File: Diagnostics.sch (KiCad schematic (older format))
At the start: 32 parts

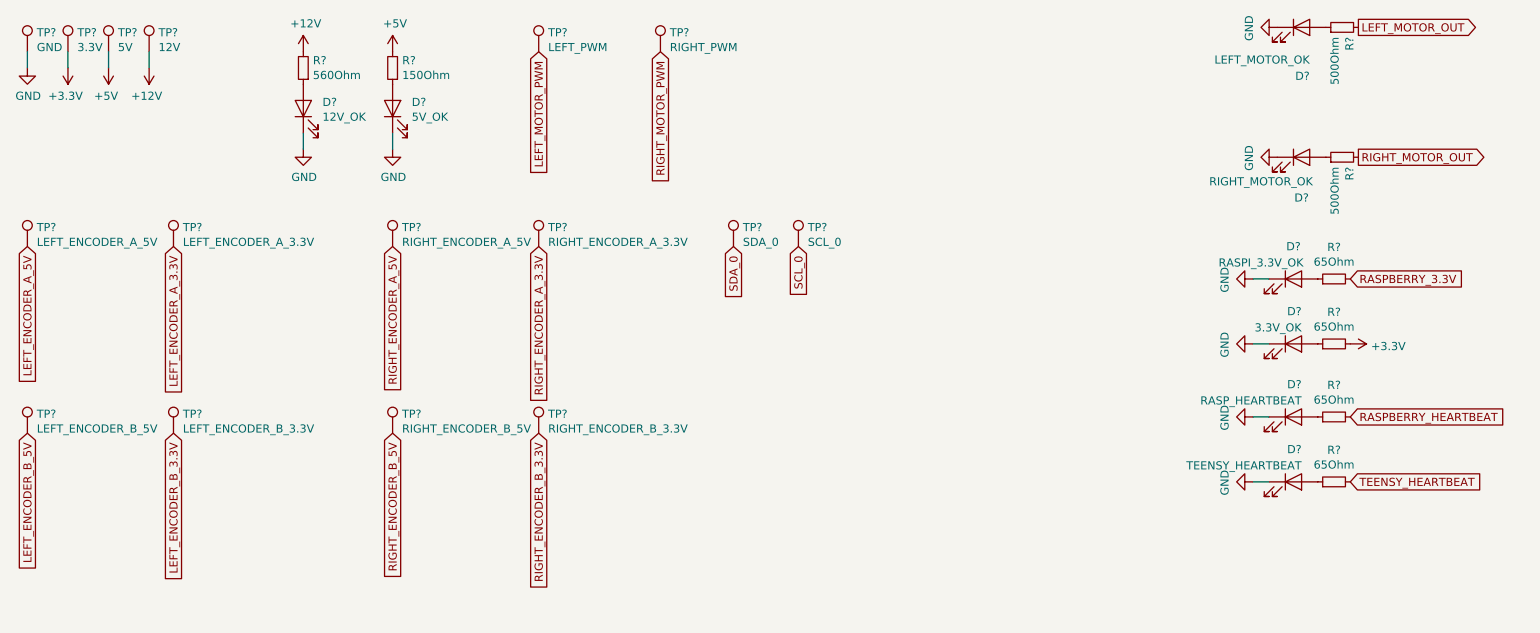
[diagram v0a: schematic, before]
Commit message: Added footprints
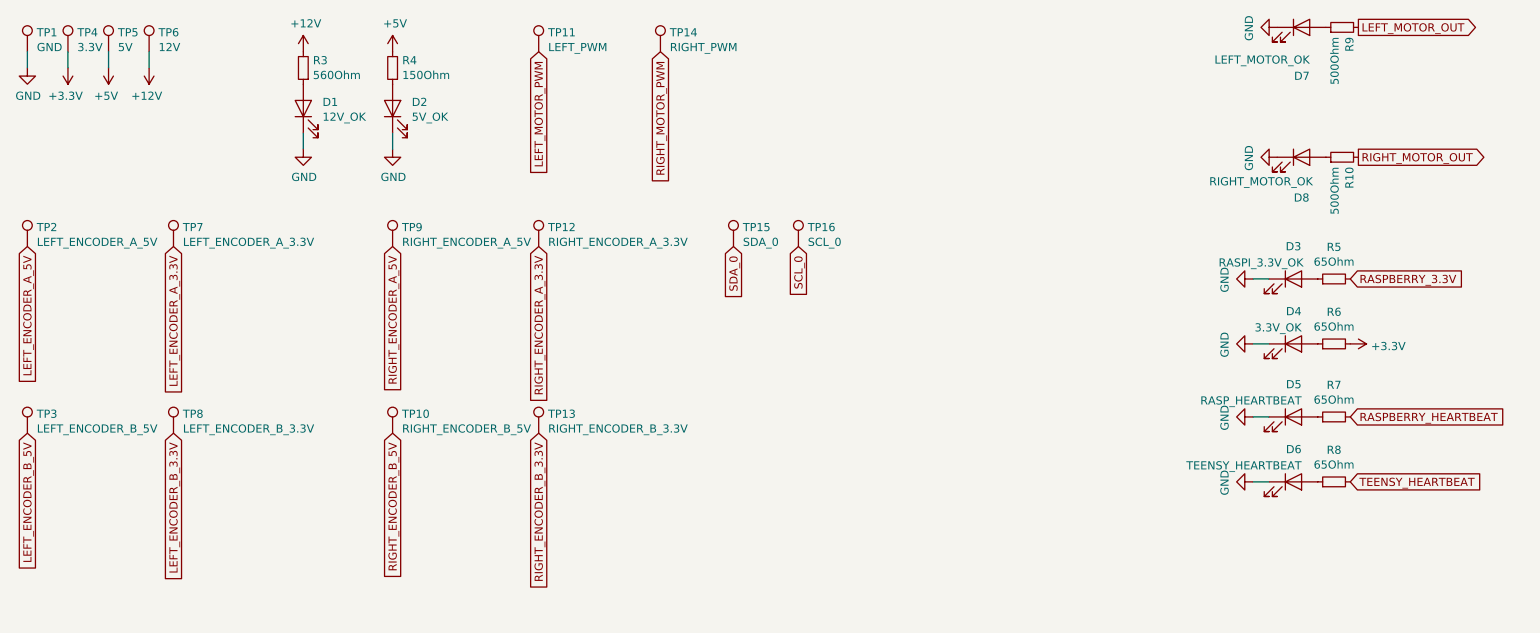
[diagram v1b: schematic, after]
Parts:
- gave numbers to parts that had none: 32

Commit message: Added footprints
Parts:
- D1, D2, D3, D4, D5, D6, D7, D8: footprint (none) -> LED_SMD:LED_0603_1608Metric_Pad1.05x0.95mm_HandSolder
- R10, R3, R4, R5, R6, R7, R8, R9: footprint (none) -> Resistor_SMD:R_0603_1608Metric_Pad1.05x0.95mm_HandSolder
- TP1, TP10, TP11, TP12, TP13, TP14, TP15, TP16, TP2, TP3, TP4, TP5, TP6, TP7, TP8, TP9: footprint (none) -> TestPoint:TestPoint_Pad_D1.5mm
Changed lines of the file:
@@
 F 0 "D1" V 2889 1582 50  0000 R CNN
 F 1 "12V_OK" V 2798 1582 50  0000 R CNN
-F 2 "" H 2850 1700 50  0001 C CNN
+F 2 "LED_SMD:LED_0603_1608Metric_Pad1.05x0.95mm_HandSolder" H 2850 1700 50  0001 C CNN
 F 3 "~" H 2850 1700 50  0001 C CNN
 	1    2850 1700
@@
 F 0 "R3" H 2791 1404 50  0000 R CNN
 F 1 "560Ohm" H 2791 1495 50  0000 R CNN
-F 2 "" H 2850 1450 50  0001 C CNN
+F 2 "Resistor_SMD:R_0603_1608Metric_Pad1.05x0.95mm_HandSolder" H 2850 1450 50  0001 C CNN
 F 3 "~" H 2850 1450 50  0001 C CNN
 	1    2850 1450
@@
 F 0 "D2" V 3439 1582 50  0000 R CNN
 F 1 "5V_OK" V 3348 1582 50  0000 R CNN
-F 2 "" H 3400 1700 50  0001 C CNN
+F 2 "LED_SMD:LED_0603_1608Metric_Pad1.05x0.95mm_HandSolder" H 3400 1700 50  0001 C CNN
 F 3 "~" H 3400 1700 50  0001 C CNN
 	1    3400 1700
@@
 F 0 "R4" H 3341 1404 50  0000 R CNN
 F 1 "150Ohm" H 3341 1495 50  0000 R CNN
-F 2 "" H 3400 1450 50  0001 C CNN
+F 2 "Resistor_SMD:R_0603_1608Metric_Pad1.05x0.95mm_HandSolder" H 3400 1450 50  0001 C CNN
 F 3 "~" H 3400 1450 50  0001 C CNN
 	1    3400 1450
@@
 F 0 "TP1" H 1208 1468 50  0000 L CNN
 F 1 "GND" H 1208 1377 50  0000 L CNN
-F 2 "" H 1350 1350 50  0001 C CNN
+F 2 "TestPoint:TestPoint_Pad_D1.5mm" H 1350 1350 50  0001 C CNN
 F 3 "~" H 1350 1350 50  0001 C CNN
 	1    1150 1350
@@
 F 0 "TP4" H 1458 1468 50  0000 L CNN
 F 1 "3.3V" H 1458 1377 50  0000 L CNN
-F 2 "" H 1600 1350 50  0001 C CNN
+F 2 "TestPoint:TestPoint_Pad_D1.5mm" H 1600 1350 50  0001 C CNN
 F 3 "~" H 1600 1350 50  0001 C CNN
 	1    1400 1350
@@
 F 0 "TP5" H 1708 1468 50  0000 L CNN
 F 1 "5V" H 1708 1377 50  0000 L CNN
-F 2 "" H 1850 1350 50  0001 C CNN
+F 2 "TestPoint:TestPoint_Pad_D1.5mm" H 1850 1350 50  0001 C CNN
 F 3 "~" H 1850 1350 50  0001 C CNN
 	1    1650 1350
@@
 F 0 "TP6" H 1958 1468 50  0000 L CNN
 F 1 "12V" H 1958 1377 50  0000 L CNN
-F 2 "" H 2100 1350 50  0001 C CNN
+F 2 "TestPoint:TestPoint_Pad_D1.5mm" H 2100 1350 50  0001 C CNN
 F 3 "~" H 2100 1350 50  0001 C CNN
 	1    1900 1350
@@
 F 0 "TP11" H 4358 1468 50  0000 L CNN
 F 1 "LEFT_PWM" H 4358 1377 50  0000 L CNN
-F 2 "" H 4500 1350 50  0001 C CNN
+F 2 "TestPoint:TestPoint_Pad_D1.5mm" H 4500 1350 50  0001 C CNN
 F 3 "~" H 4500 1350 50  0001 C CNN
 	1    4300 1350
@@
 F 0 "TP14" H 5108 1468 50  0000 L CNN
 F 1 "RIGHT_PWM" H 5108 1377 50  0000 L CNN
-F 2 "" H 5250 1350 50  0001 C CNN
+F 2 "TestPoint:TestPoint_Pad_D1.5mm" H 5250 1350 50  0001 C CNN
 F 3 "~" H 5250 1350 50  0001 C CNN
 	1    5050 1350
@@
 F 0 "R9" H 9191 1154 50  0000 R CNN
 F 1 "500Ohm" H 9191 1245 50  0000 R CNN
-F 2 "" H 9250 1200 50  0001 C CNN
+F 2 "Resistor_SMD:R_0603_1608Metric_Pad1.05x0.95mm_HandSolder" H 9250 1200 50  0001 C CNN
 F 3 "~" H 9250 1200 50  0001 C CNN
 	1    9250 1200
@@
 F 0 "D7" H 9050 900 50  0000 R CNN
 F 1 "LEFT_MOTOR_OK" H 9050 1000 50  0000 R CNN
-F 2 "" H 9000 1200 50  0001 C CNN
+F 2 "LED_SMD:LED_0603_1608Metric_Pad1.05x0.95mm_HandSolder" H 9000 1200 50  0001 C CNN
 F 3 "~" H 9000 1200 50  0001 C CNN
 	1    9000 1200
@@
 F 0 "R10" H 9191 1954 50  0000 R CNN
 F 1 "500Ohm" H 9191 2045 50  0000 R CNN
-F 2 "" H 9250 2000 50  0001 C CNN
+F 2 "Resistor_SMD:R_0603_1608Metric_Pad1.05x0.95mm_HandSolder" H 9250 2000 50  0001 C CNN
 F 3 "~" H 9250 2000 50  0001 C CNN
 	1    9250 2000
@@
 F 0 "D8" H 9000 1750 50  0000 C CNN
 F 1 "RIGHT_MOTOR_OK" H 8750 1850 50  0000 C CNN
-F 2 "" H 9000 2000 50  0001 C CNN
+F 2 "LED_SMD:LED_0603_1608Metric_Pad1.05x0.95mm_HandSolder" H 9000 2000 50  0001 C CNN
 F 3 "~" H 9000 2000 50  0001 C CNN
 	1    9000 2000
@@
 F 0 "TP2" H 1208 2668 50  0000 L CNN
 F 1 "LEFT_ENCODER_A_5V" H 1208 2577 50  0000 L CNN
-F 2 "" H 1350 2550 50  0001 C CNN
+F 2 "TestPoint:TestPoint_Pad_D1.5mm" H 1350 2550 50  0001 C CNN
 F 3 "~" H 1350 2550 50  0001 C CNN
 	1    1150 2550
@@
 F 0 "TP7" H 2108 2668 50  0000 L CNN
 F 1 "LEFT_ENCODER_A_3.3V" H 2108 2577 50  0000 L CNN
-F 2 "" H 2250 2550 50  0001 C CNN
+F 2 "TestPoint:TestPoint_Pad_D1.5mm" H 2250 2550 50  0001 C CNN
 F 3 "~" H 2250 2550 50  0001 C CNN
 	1    2050 2550
@@
 F 0 "TP3" H 1208 3818 50  0000 L CNN
 F 1 "LEFT_ENCODER_B_5V" H 1208 3727 50  0000 L CNN
-F 2 "" H 1350 3700 50  0001 C CNN
+F 2 "TestPoint:TestPoint_Pad_D1.5mm" H 1350 3700 50  0001 C CNN
 F 3 "~" H 1350 3700 50  0001 C CNN
 	1    1150 3700
@@
 F 0 "TP8" H 2108 3818 50  0000 L CNN
 F 1 "LEFT_ENCODER_B_3.3V" H 2108 3727 50  0000 L CNN
-F 2 "" H 2250 3700 50  0001 C CNN
+F 2 "TestPoint:TestPoint_Pad_D1.5mm" H 2250 3700 50  0001 C CNN
 F 3 "~" H 2250 3700 50  0001 C CNN
 	1    2050 3700
@@
 F 0 "TP9" H 3458 2668 50  0000 L CNN
 F 1 "RIGHT_ENCODER_A_5V" H 3458 2577 50  0000 L CNN
-F 2 "" H 3600 2550 50  0001 C CNN
+F 2 "TestPoint:TestPoint_Pad_D1.5mm" H 3600 2550 50  0001 C CNN
 F 3 "~" H 3600 2550 50  0001 C CNN
 	1    3400 2550
@@
 F 0 "TP12" H 4358 2668 50  0000 L CNN
 F 1 "RIGHT_ENCODER_A_3.3V" H 4358 2577 50  0000 L CNN
-F 2 "" H 4500 2550 50  0001 C CNN
+F 2 "TestPoint:TestPoint_Pad_D1.5mm" H 4500 2550 50  0001 C CNN
 F 3 "~" H 4500 2550 50  0001 C CNN
 	1    4300 2550
@@
 F 0 "TP10" H 3458 3818 50  0000 L CNN
 F 1 "RIGHT_ENCODER_B_5V" H 3458 3727 50  0000 L CNN
-F 2 "" H 3600 3700 50  0001 C CNN
+F 2 "TestPoint:TestPoint_Pad_D1.5mm" H 3600 3700 50  0001 C CNN
 F 3 "~" H 3600 3700 50  0001 C CNN
 	1    3400 3700
@@
 F 0 "TP13" H 4358 3818 50  0000 L CNN
 F 1 "RIGHT_ENCODER_B_3.3V" H 4358 3727 50  0000 L CNN
-F 2 "" H 4500 3700 50  0001 C CNN
+F 2 "TestPoint:TestPoint_Pad_D1.5mm" H 4500 3700 50  0001 C CNN
 F 3 "~" H 4500 3700 50  0001 C CNN
 	1    4300 3700
@@
 F 0 "R5" V 9396 2750 50  0000 C CNN
 F 1 "65Ohm" V 9305 2750 50  0000 C CNN
-F 2 "" H 9200 2750 50  0001 C CNN
+F 2 "Resistor_SMD:R_0603_1608Metric_Pad1.05x0.95mm_HandSolder" H 9200 2750 50  0001 C CNN
 F 3 "~" H 9200 2750 50  0001 C CNN
 	1    9200 2750
@@
 F 0 "D4" H 9000 3350 50  0000 R CNN
 F 1 "3.3V_OK" H 9000 3250 50  0000 R CNN
-F 2 "" H 8950 3150 50  0001 C CNN
+F 2 "LED_SMD:LED_0603_1608Metric_Pad1.05x0.95mm_HandSolder" H 8950 3150 50  0001 C CNN
 F 3 "~" H 8950 3150 50  0001 C CNN
 	1    8950 3150
@@
 F 0 "R6" V 9396 3150 50  0000 C CNN
 F 1 "65Ohm" V 9305 3150 50  0000 C CNN
-F 2 "" H 9200 3150 50  0001 C CNN
+F 2 "Resistor_SMD:R_0603_1608Metric_Pad1.05x0.95mm_HandSolder" H 9200 3150 50  0001 C CNN
 F 3 "~" H 9200 3150 50  0001 C CNN
 	1    9200 3150
@@
 F 0 "D3" H 8950 2950 50  0000 C CNN
 F 1 "RASPI_3.3V_OK" H 8750 2850 50  0000 C CNN
-F 2 "" H 8950 2750 50  0001 C CNN
+F 2 "LED_SMD:LED_0603_1608Metric_Pad1.05x0.95mm_HandSolder" H 8950 2750 50  0001 C CNN
 F 3 "~" H 8950 2750 50  0001 C CNN
 	1    8950 2750
@@
 F 0 "D5" H 9000 3800 50  0000 R CNN
 F 1 "RASP_HEARTBEAT" H 9000 3700 50  0000 R CNN
-F 2 "" H 8950 3600 50  0001 C CNN
+F 2 "LED_SMD:LED_0603_1608Metric_Pad1.05x0.95mm_HandSolder" H 8950 3600 50  0001 C CNN
 F 3 "~" H 8950 3600 50  0001 C CNN
 	1    8950 3600
@@
 F 0 "R7" V 9396 3600 50  0000 C CNN
 F 1 "65Ohm" V 9305 3600 50  0000 C CNN
-F 2 "" H 9200 3600 50  0001 C CNN
+F 2 "Resistor_SMD:R_0603_1608Metric_Pad1.05x0.95mm_HandSolder" H 9200 3600 50  0001 C CNN
 F 3 "~" H 9200 3600 50  0001 C CNN
 	1    9200 3600
@@
 F 0 "D6" H 9000 4200 50  0000 R CNN
 F 1 "TEENSY_HEARTBEAT" H 9000 4100 50  0000 R CNN
-F 2 "" H 8950 4000 50  0001 C CNN
+F 2 "LED_SMD:LED_0603_1608Metric_Pad1.05x0.95mm_HandSolder" H 8950 4000 50  0001 C CNN
 F 3 "~" H 8950 4000 50  0001 C CNN
 	1    8950 4000
@@
 F 0 "R8" V 9396 4000 50  0000 C CNN
 F 1 "65Ohm" V 9305 4000 50  0000 C CNN
-F 2 "" H 9200 4000 50  0001 C CNN
+F 2 "Resistor_SMD:R_0603_1608Metric_Pad1.05x0.95mm_HandSolder" H 9200 4000 50  0001 C CNN
 F 3 "~" H 9200 4000 50  0001 C CNN
 	1    9200 4000
@@
 F 0 "TP15" H 5558 2668 50  0000 L CNN
 F 1 "SDA_0" H 5558 2577 50  0000 L CNN
-F 2 "" H 5700 2550 50  0001 C CNN
+F 2 "TestPoint:TestPoint_Pad_D1.5mm" H 5700 2550 50  0001 C CNN
 F 3 "~" H 5700 2550 50  0001 C CNN
 	1    5500 2550
@@
 F 0 "TP16" H 5958 2668 50  0000 L CNN
 F 1 "SCL_0" H 5958 2577 50  0000 L CNN
-F 2 "" H 6100 2550 50  0001 C CNN
+F 2 "TestPoint:TestPoint_Pad_D1.5mm" H 6100 2550 50  0001 C CNN
 F 3 "~" H 6100 2550 50  0001 C CNN
 	1    5900 2550

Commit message: Added BOM
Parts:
- D1, D2, D3, D4, D5, D6, D7, D8: DigiKey (none) -> 516-1421-1-ND
- R10, R3, R9: DigiKey (none) -> RR08P560DCT-ND
- R4: DigiKey (none) -> 311-150HRCT-ND
- R5, R6, R7, R8: DigiKey (none) -> 2019-RK73B1JTTD111JCT-ND
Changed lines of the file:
@@
 F 2 "LED_SMD:LED_0603_1608Metric_Pad1.05x0.95mm_HandSolder" H 2850 1700 50  0001 C CNN
 F 3 "~" H 2850 1700 50  0001 C CNN
+F 4 "516-1421-1-ND" H 2850 1700 50  0001 C CNN "DigiKey"
 	1    2850 1700
 	0    -1   -1   0
@@
 F 2 "Resistor_SMD:R_0603_1608Metric_Pad1.05x0.95mm_HandSolder" H 2850 1450 50  0001 C CNN
 F 3 "~" H 2850 1450 50  0001 C CNN
+F 4 " RR08P560DCT-ND " H 2850 1450 50  0001 C CNN "DigiKey"
 	1    2850 1450
 	-1   0    0    1
@@
 F 2 "LED_SMD:LED_0603_1608Metric_Pad1.05x0.95mm_HandSolder" H 3400 1700 50  0001 C CNN
 F 3 "~" H 3400 1700 50  0001 C CNN
+F 4 "516-1421-1-ND" H 3400 1700 50  0001 C CNN "DigiKey"
 	1    3400 1700
 	0    -1   -1   0
@@
 F 2 "Resistor_SMD:R_0603_1608Metric_Pad1.05x0.95mm_HandSolder" H 3400 1450 50  0001 C CNN
 F 3 "~" H 3400 1450 50  0001 C CNN
+F 4 " 311-150HRCT-ND " H 3400 1450 50  0001 C CNN "DigiKey"
 	1    3400 1450
 	-1   0    0    1
@@
 F 2 "Resistor_SMD:R_0603_1608Metric_Pad1.05x0.95mm_HandSolder" H 9250 1200 50  0001 C CNN
 F 3 "~" H 9250 1200 50  0001 C CNN
+F 4 " RR08P560DCT-ND " H 9250 1200 50  0001 C CNN "DigiKey"
 	1    9250 1200
 	0    -1   -1   0
@@
 F 2 "LED_SMD:LED_0603_1608Metric_Pad1.05x0.95mm_HandSolder" H 9000 1200 50  0001 C CNN
 F 3 "~" H 9000 1200 50  0001 C CNN
+F 4 "516-1421-1-ND" H 9000 1200 50  0001 C CNN "DigiKey"
 	1    9000 1200
 	1    0    0    -1
@@
 F 2 "Resistor_SMD:R_0603_1608Metric_Pad1.05x0.95mm_HandSolder" H 9250 2000 50  0001 C CNN
 F 3 "~" H 9250 2000 50  0001 C CNN
+F 4 " RR08P560DCT-ND " H 9250 2000 50  0001 C CNN "DigiKey"
 	1    9250 2000
 	0    -1   -1   0
@@
 F 2 "LED_SMD:LED_0603_1608Metric_Pad1.05x0.95mm_HandSolder" H 9000 2000 50  0001 C CNN
 F 3 "~" H 9000 2000 50  0001 C CNN
+F 4 "516-1421-1-ND" H 9000 2000 50  0001 C CNN "DigiKey"
 	1    9000 2000
 	1    0    0    -1
@@
 F 2 "Resistor_SMD:R_0603_1608Metric_Pad1.05x0.95mm_HandSolder" H 9200 2750 50  0001 C CNN
 F 3 "~" H 9200 2750 50  0001 C CNN
+F 4 " 2019-RK73B1JTTD111JCT-ND " H 9200 2750 50  0001 C CNN "DigiKey"
 	1    9200 2750
 	0    -1   -1   0
@@
 F 2 "LED_SMD:LED_0603_1608Metric_Pad1.05x0.95mm_HandSolder" H 8950 3150 50  0001 C CNN
 F 3 "~" H 8950 3150 50  0001 C CNN
+F 4 "516-1421-1-ND" H 8950 3150 50  0001 C CNN "DigiKey"
 	1    8950 3150
 	1    0    0    -1
@@
 F 2 "Resistor_SMD:R_0603_1608Metric_Pad1.05x0.95mm_HandSolder" H 9200 3150 50  0001 C CNN
 F 3 "~" H 9200 3150 50  0001 C CNN
+F 4 " 2019-RK73B1JTTD111JCT-ND " H 9200 3150 50  0001 C CNN "DigiKey"
 	1    9200 3150
 	0    -1   -1   0
@@
 F 2 "LED_SMD:LED_0603_1608Metric_Pad1.05x0.95mm_HandSolder" H 8950 2750 50  0001 C CNN
 F 3 "~" H 8950 2750 50  0001 C CNN
+F 4 "516-1421-1-ND" H 8950 2750 50  0001 C CNN "DigiKey"
 	1    8950 2750
 	1    0    0    -1
@@
 F 2 "LED_SMD:LED_0603_1608Metric_Pad1.05x0.95mm_HandSolder" H 8950 3600 50  0001 C CNN
 F 3 "~" H 8950 3600 50  0001 C CNN
+F 4 "516-1421-1-ND" H 8950 3600 50  0001 C CNN "DigiKey"
 	1    8950 3600
 	1    0    0    -1
@@
 F 2 "Resistor_SMD:R_0603_1608Metric_Pad1.05x0.95mm_HandSolder" H 9200 3600 50  0001 C CNN
 F 3 "~" H 9200 3600 50  0001 C CNN
+F 4 " 2019-RK73B1JTTD111JCT-ND " H 9200 3600 50  0001 C CNN "DigiKey"
 	1    9200 3600
 	0    -1   -1   0
@@
 F 2 "LED_SMD:LED_0603_1608Metric_Pad1.05x0.95mm_HandSolder" H 8950 4000 50  0001 C CNN
 F 3 "~" H 8950 4000 50  0001 C CNN
+F 4 "516-1421-1-ND" H 8950 4000 50  0001 C CNN "DigiKey"
 	1    8950 4000
 	1    0    0    -1
@@
 F 2 "Resistor_SMD:R_0603_1608Metric_Pad1.05x0.95mm_HandSolder" H 9200 4000 50  0001 C CNN
 F 3 "~" H 9200 4000 50  0001 C CNN
+F 4 " 2019-RK73B1JTTD111JCT-ND " H 9200 4000 50  0001 C CNN "DigiKey"
 	1    9200 4000
 	0    -1   -1   0

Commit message: Most of rev B
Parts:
- added D13: TEENSY_DEBUG, LED_SMD:LED_0603_1608Metric_Pad1.05x0.95mm_HandSolder, symbol Device:LED
- added R63: 65Ohm, Resistor_SMD:R_0603_1608Metric_Pad1.05x0.95mm_HandSolder, symbol Device:R_Small
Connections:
- net GND: now also D13.1 (K)
- new net: D13.2 (A), R63.1
- new net TEENSY_DEBUG: R63.2
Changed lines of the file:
@@
 $Descr A4 11693 8268
 encoding utf-8
-Sheet 2 4
+Sheet 2 6
 Title ""
 Date ""
@@
 	1    0    0    -1
 $EndComp
+$Comp
+L Device:LED D?
+U 1 1 5F5638C4
+P 8950 4400
+AR Path="/5F5638C4" Ref="D?"  Part="1"
+AR Path="/5DF0C54F/5F5638C4" Ref="D13"  Part="1"
+F 0 "D13" H 9000 4600 50  0000 R CNN
+F 1 "TEENSY_DEBUG" H 9000 4500 50  0000 R CNN
+F 2 "LED_SMD:LED_0603_1608Metric_Pad1.05x0.95mm_HandSolder" H 8950 4400 50  0001 C CNN
+F 3 "~" H 8950 4400 50  0001 C CNN
+F 4 "516-1421-1-ND" H 8950 4400 50  0001 C CNN "DigiKey"
+	1    8950 4400
+	1    0    0    -1
+$EndComp
+$Comp
+L Device:R_Small R?
+U 1 1 5F5638CF
+P 9200 4400
+AR Path="/5F5638CF" Ref="R?"  Part="1"
+AR Path="/5DF0C54F/5F5638CF" Ref="R63"  Part="1"
+F 0 "R63" V 9396 4400 50  0000 C CNN
+F 1 "65Ohm" V 9305 4400 50  0000 C CNN
+F 2 "Resistor_SMD:R_0603_1608Metric_Pad1.05x0.95mm_HandSolder" H 9200 4400 50  0001 C CNN
+F 3 "~" H 9200 4400 50  0001 C CNN
+F 4 " 2019-RK73B1JTTD111JCT-ND " H 9200 4400 50  0001 C CNN "DigiKey"
+	1    9200 4400
+	0    -1   -1   0
+$EndComp
+$Comp
+L power:GND #PWR?
+U 1 1 5F5638D9
+P 8700 4400
+AR Path="/5F5638D9" Ref="#PWR?"  Part="1"
+AR Path="/5DF0C54F/5F5638D9" Ref="#PWR0253"  Part="1"
+F 0 "#PWR0253" H 8700 4150 50  0001 C CNN
+F 1 "GND" H 8705 4227 50  0000 C CNN
+F 2 "" H 8700 4400 50  0001 C CNN
+F 3 "" H 8700 4400 50  0001 C CNN
+	1    8700 4400
+	0    1    1    0
+$EndComp
+Wire Wire Line
+	8700 4400 8800 4400
+Text GLabel 9300 4400 2    50   Input ~ 0
+TEENSY_DEBUG
 $EndSCHEMATC
